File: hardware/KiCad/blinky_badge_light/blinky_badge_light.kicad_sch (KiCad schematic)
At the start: 12 parts, among them U1 ESP32-S3-WROOM-1

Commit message: updated schematic to use 'basic' parts from jlcpcb where I could
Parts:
- C39: JLCPCB Part # C2762594 -> C59461
- C40: JLCPCB Part # C1848 -> C15849
- R1: JLCPCB Part # C105882 -> C22775
- R11, R12: JLCPCB Part # C98220 -> C25804
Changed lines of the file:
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@@
 			)
 		)
-		(property "Datasheet" "https://www.lcsc.com/datasheet/lcsc_datasheet_2304140030_Samsung-Electro-Mechanics-CL31B105KBHNNNE_C1848.pdf"
+		(property "Datasheet" "https://jlcpcb.com/api/file/downloadByFileSystemAccessId/8556213788459761664"
 			(at 88.9 48.26 0)
 			(effects
@@
 			)
 		)
-		(property "JLCPCB Part #" "C1848"
+		(property "JLCPCB Part #" "C15849"
 			(at 88.9 48.26 0)
 			(effects
@@
 			)
 		)
-		(property "Datasheet" "https://www.lcsc.com/datasheet/lcsc_datasheet_2304140030_YAGEO-RC0603FR-0710KL_C98220.pdf"
+		(property "Datasheet" "https://jlcpcb.com/api/file/downloadByFileSystemAccessId/8579706381320323072"
 			(at 224.79 63.5 0)
 			(effects
@@
 			)
 		)
-		(property "JLCPCB Part #" "C98220"
+		(property "JLCPCB Part #" "C25804"
 			(at 224.79 63.5 0)
 			(effects
@@
 			)
 		)
-		(property "Datasheet" "https://www.lcsc.com/datasheet/lcsc_datasheet_2304140030_YAGEO-RC0603FR-0710KL_C98220.pdf"
+		(property "Datasheet" "https://jlcpcb.com/api/file/downloadByFileSystemAccessId/8579706381320323072"
 			(at 105.41 45.72 0)
 			(effects
@@
 			)
 		)
-		(property "JLCPCB Part #" "C98220"
+		(property "JLCPCB Part #" "C25804"
 			(at 105.41 45.72 0)
 			(effects
@@
 			)
 		)
-		(property "Datasheet" "https://www.lcsc.com/datasheet/lcsc_datasheet_2208111030_Samsung-Electro-Mechanics-CL10A226MO7JZNC_C2762594.pdf"
+		(property "Datasheet" "https://jlcpcb.com/api/file/downloadByFileSystemAccessId/8555544417670705152"
 			(at 128.27 30.48 0)
 			(effects
@@
 			)
 		)
-		(property "JLCPCB Part #" "C2762594"
+		(property "JLCPCB Part #" "C59461"
 			(at 128.27 30.48 0)
 			(effects
@@
 			)
 		)
-		(property "Datasheet" "https://www.lcsc.com/datasheet/lcsc_datasheet_2407081117_YAGEO-CC0402KRX5R9BB104_C105882.pdf"
+		(property "Datasheet" "https://jlcpcb.com/api/file/downloadByFileSystemAccessId/8579706114222985216"
 			(at 218.44 76.2 0)
 			(effects
@@
 			)
 		)
-		(property "JLCPCB Part #" "C105882"
+		(property "JLCPCB Part #" "C22775"
 			(at 218.44 76.2 0)
 			(effects

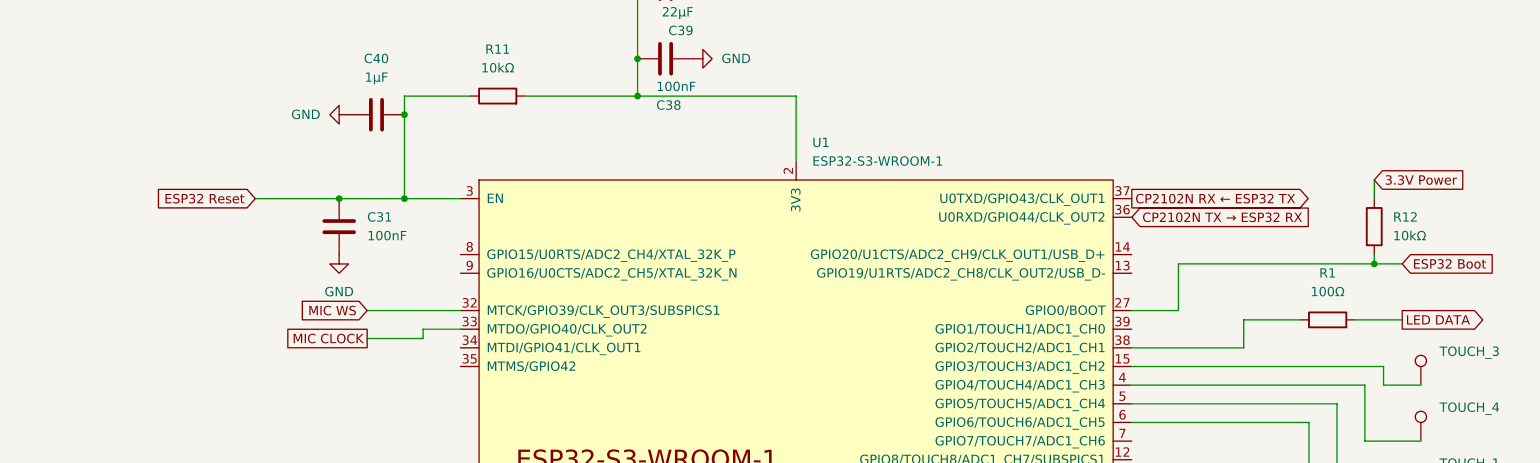
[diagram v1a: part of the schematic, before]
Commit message: swap esp32 boot and reset's connections to CP2102
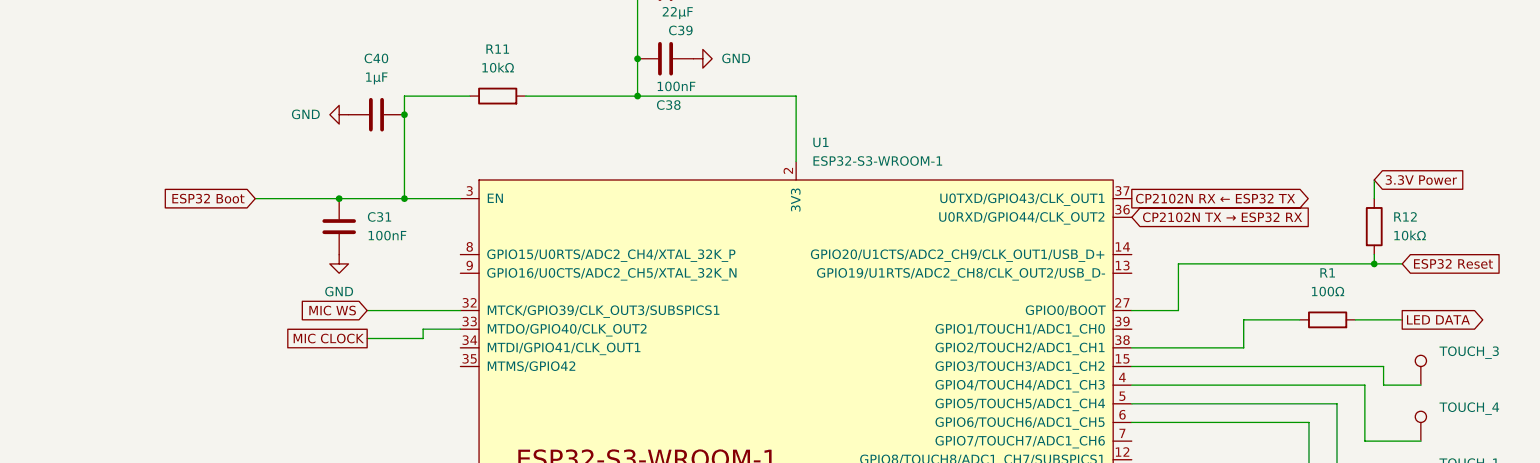
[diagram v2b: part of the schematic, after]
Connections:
- net ESP32 Boot: now also C31.2, C40.2, R11.1, U1.3 (EN); no longer R12.2, U1.27 (GPIO0/BOOT)
- net ESP32 Reset: now also R12.2, U1.27 (GPIO0/BOOT); no longer C31.2, C40.2, R11.1, U1.3 (EN)
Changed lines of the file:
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@@
 		)
 	)
-	(global_label "ESP32 Boot"
+	(global_label "ESP32 Reset"
 		(shape input)
 		(at 228.6 68.58 0)
@@
 		)
 		(property "Intersheetrefs" "${INTERSHEET_REFS}"
-			(at 242.894 68.58 0)
+			(at 243.8013 68.58 0)
 			(effects
 				(font
@@
 		)
 	)
-	(global_label "ESP32 Reset"
+	(global_label "ESP32 Boot"
 		(shape input)
 		(at 72.39 59.69 180)
@@
 		)
 		(property "Intersheetrefs" "${INTERSHEET_REFS}"
-			(at 57.1887 59.69 0)
+			(at 58.096 59.69 0)
 			(effects
 				(font

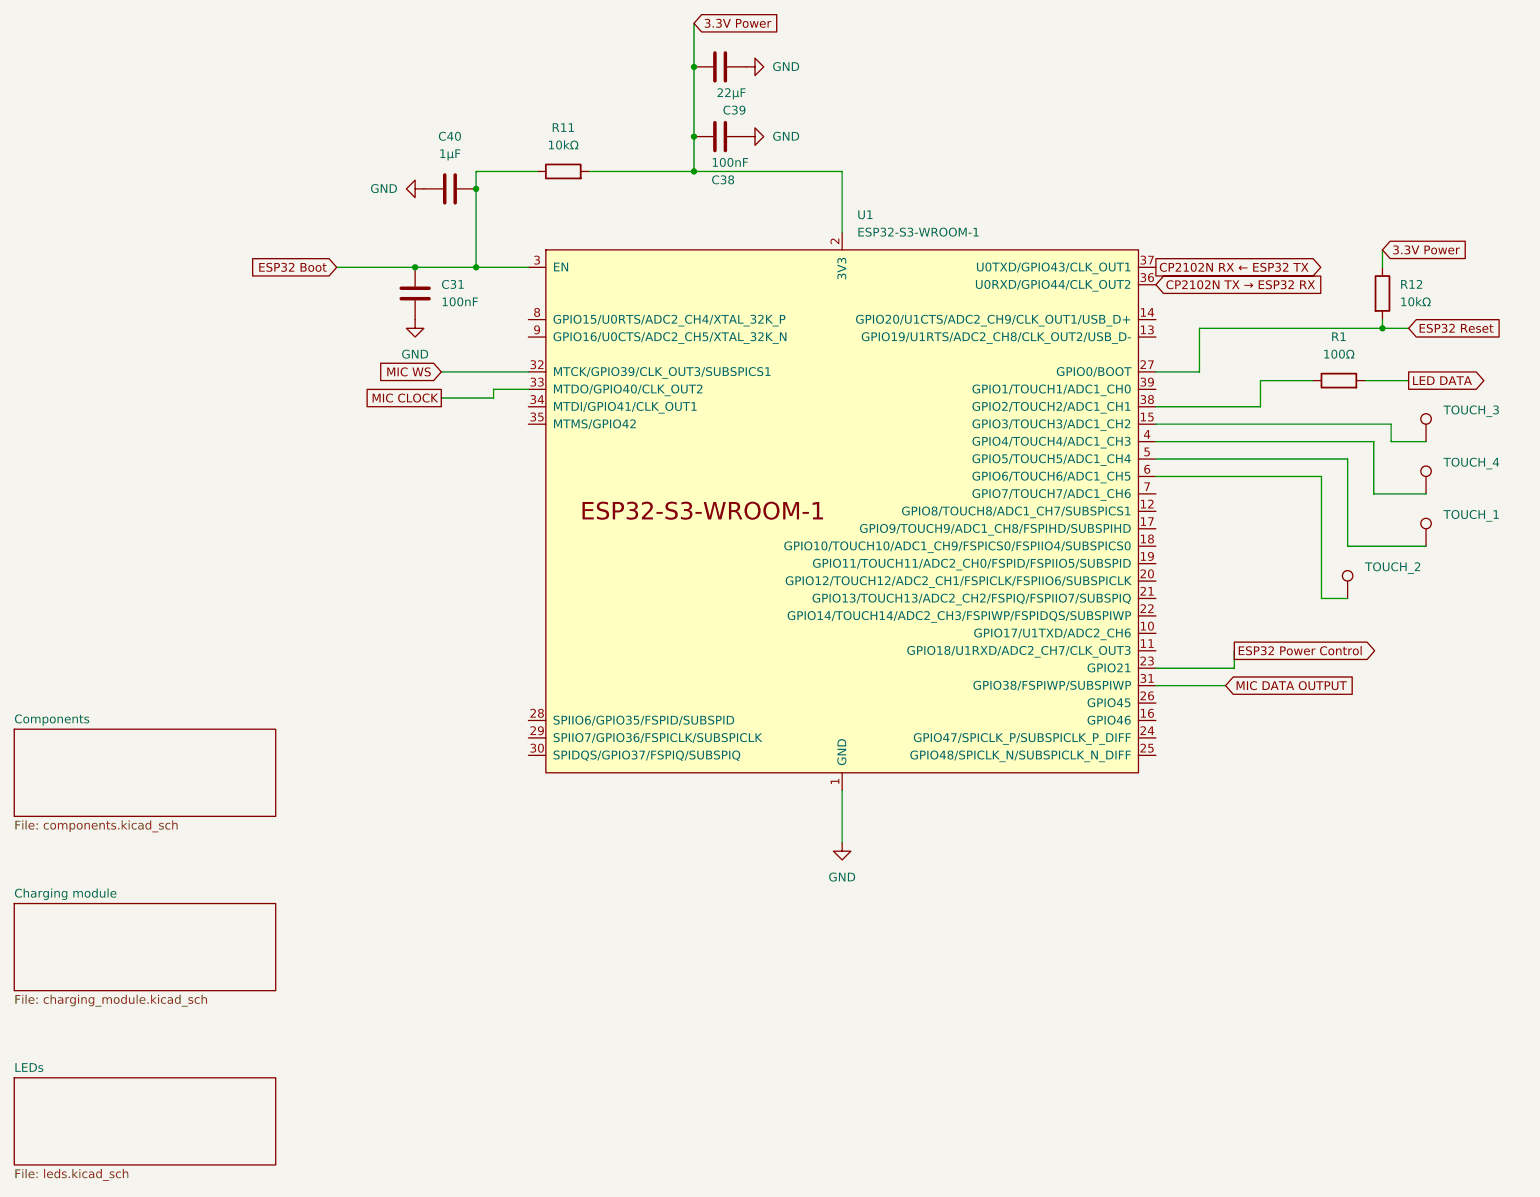
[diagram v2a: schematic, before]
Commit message: added battery polarity protection and charging monitoring circuit
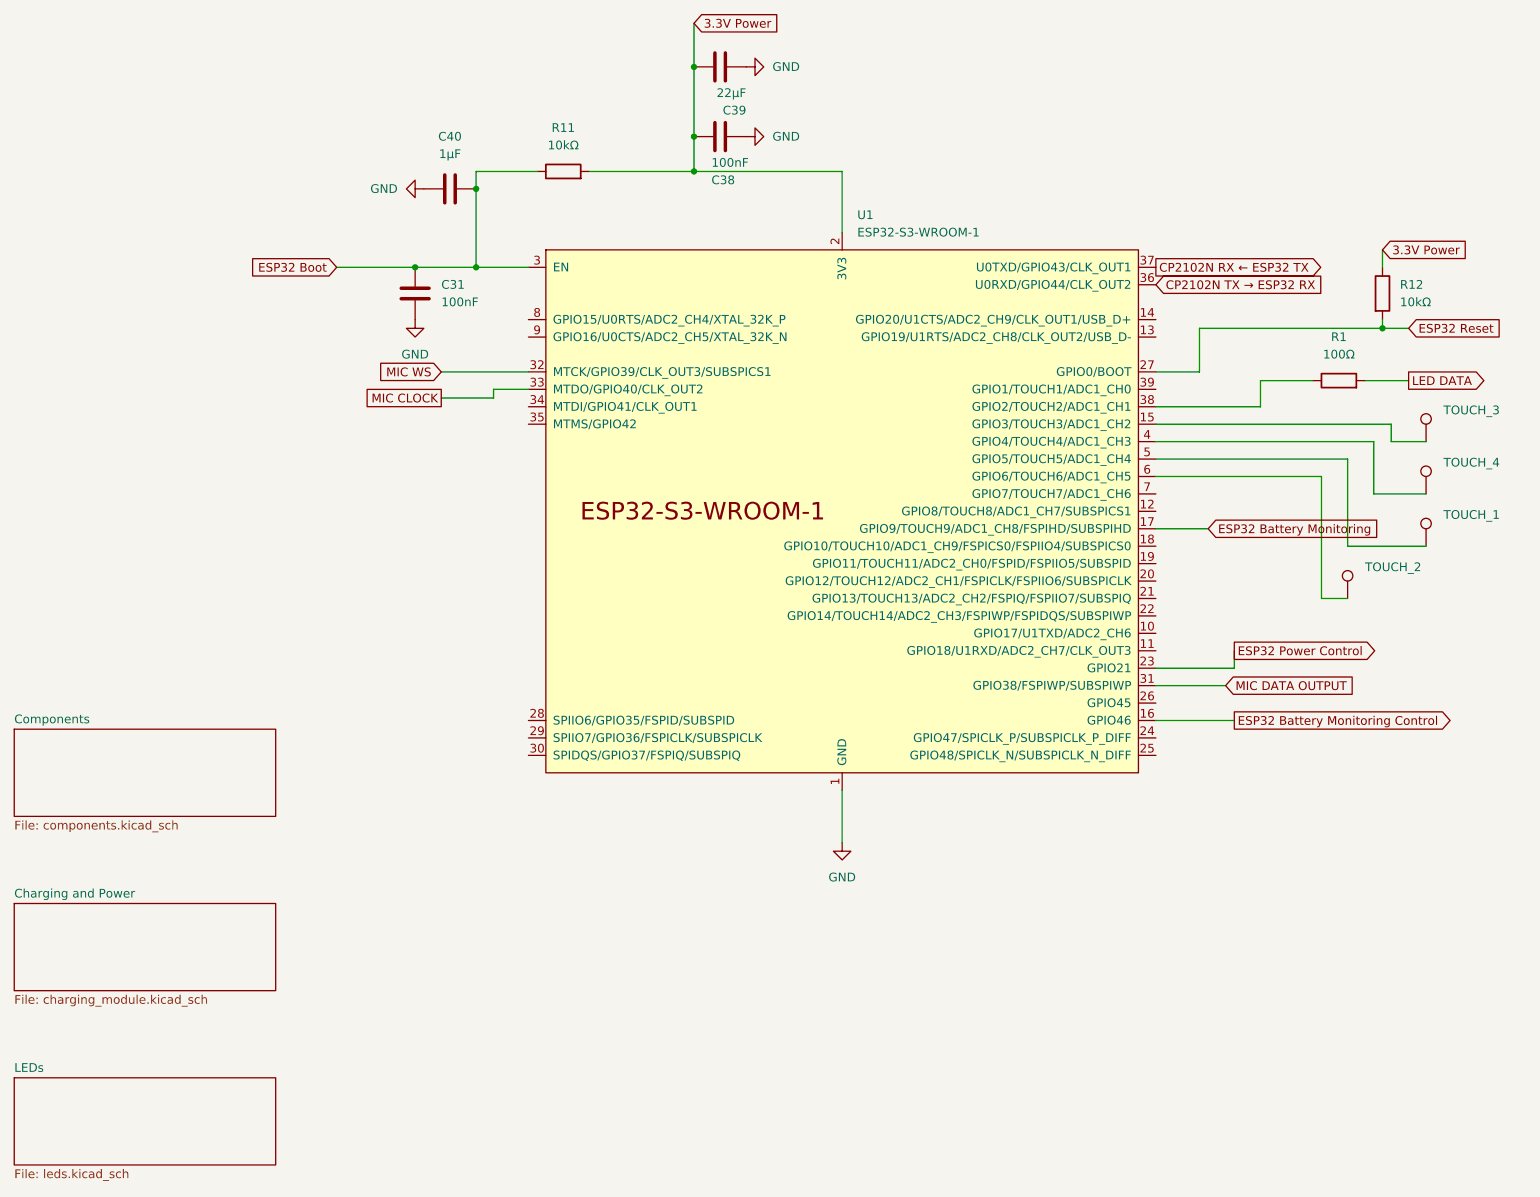
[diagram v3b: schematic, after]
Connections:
- net ESP32 Battery Monitoring Control: now reaches U1.16 (GPIO46)
- net ESP32 Battery Monitoring: now reaches U1.17 (GPIO9/TOUCH9/ADC1_CH8/FSPIHD/SUBSPIHD)
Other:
- sheet Charging module renamed Charging and Power
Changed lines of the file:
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@@
+	(wire
+		(pts
+			(xy 191.77 125.73) (xy 203.2 125.73)
+		)
+		(stroke
+			(width 0)
+			(type default)
+		)
+	)
 	(wire
 		(pts
@@
 		(pts
 			(xy 207.01 80.01) (xy 191.77 80.01)
+		)
+		(stroke
+			(width 0)
+			(type default)
+		)
+	)
+	(wire
+		(pts
+			(xy 191.77 97.79) (xy 199.39 97.79)
 		)
 		(stroke
@@
 		)
 	)
+	(global_label "ESP32 Battery Monitoring Control"
+		(shape output)
+		(at 203.2 125.73 0)
+		(fields_autoplaced yes)
+		(effects
+			(font
+				(size 1.27 1.27)
+			)
+			(justify left)
+		)
+		(property "Intersheetrefs" "${INTERSHEET_REFS}"
+			(at 238.6603 125.73 0)
+			(effects
+				(font
+					(size 1.27 1.27)
+				)
+				(justify left)
+				(hide yes)
+			)
+		)
+	)
 	(global_label "LED DATA"
 		(shape output)
@@
 		(property "Intersheetrefs" "${INTERSHEET_REFS}"
 			(at 221.7881 120.65 0)
+			(effects
+				(font
+					(size 1.27 1.27)
+				)
+				(justify left)
+				(hide yes)
+			)
+		)
+	)
+	(global_label "ESP32 Battery Monitoring"
+		(shape input)
+		(at 199.39 97.79 0)
+		(fields_autoplaced yes)
+		(effects
+			(font
+				(size 1.27 1.27)
+			)
+			(justify left)
+		)
+		(property "Intersheetrefs" "${INTERSHEET_REFS}"
+			(at 226.9886 97.79 0)
 			(effects
 				(font
@@
 			(color 0 0 0 0.0000)
 		)
-		(property "Sheetname" "Charging module"
+		(property "Sheetname" "Charging and Power"
 			(at 25.4 151.6884 0)
 			(effects

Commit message: moving some stuff around
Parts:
- added TOUCH_5: TestPoint, TestPoint:TestPoint_Pad_D4.0mm, symbol Connector:TestPoint
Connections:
- net at U1.7 (GPIO7/TOUCH7/ADC1_CH6): now also TOUCH_5.1
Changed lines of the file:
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@@
+	(wire
+		(pts
+			(xy 191.77 92.71) (xy 196.85 92.71)
+		)
+		(stroke
+			(width 0)
+			(type default)
+		)
+	)
 	(wire
 		(pts
@@
 					(unit 1)
 				)
+			)
+		)
+	)
+	(symbol
+		(lib_id "Connector:TestPoint")
+		(at 196.85 92.71 270)
+		(unit 1)
+		(exclude_from_sim no)
+		(in_bom yes)
+		(on_board yes)
+		(dnp no)
+		(property "Reference" "TOUCH_5"
+			(at 201.93 92.71 90)
+			(effects
+				(font
+					(size 1.27 1.27)
+				)
+				(justify left)
+			)
+		)
+		(property "Value" "TestPoint"
+			(at 201.93 93.9799 90)
+			(effects
+				(font
+					(size 1.27 1.27)
+				)
+				(justify left)
+				(hide yes)
+			)
+		)
+		(property "Footprint" "TestPoint:TestPoint_Pad_D4.0mm"
+			(at 196.85 97.79 0)
+			(effects
+				(font
+					(size 1.27 1.27)
+				)
+				(hide yes)
+			)
+		)
+		(property "Datasheet" "~"
+			(at 196.85 97.79 0)
+			(effects
+				(font
+					(size 1.27 1.27)
+				)
+				(hide yes)
+			)
+		)
+		(property "Description" "test point"
+			(at 196.85 92.71 0)
+			(effects
+				(font
+					(size 1.27 1.27)
+				)
+				(hide yes)
+			)
+		)
+		(pin "1"
+		)
+		(instances
+			(project ""
+				(path "/f33039b1-b38b-4cb6-baf0-07a137773378"
+					(reference "TOUCH_5")
+					(unit 1)
+				)

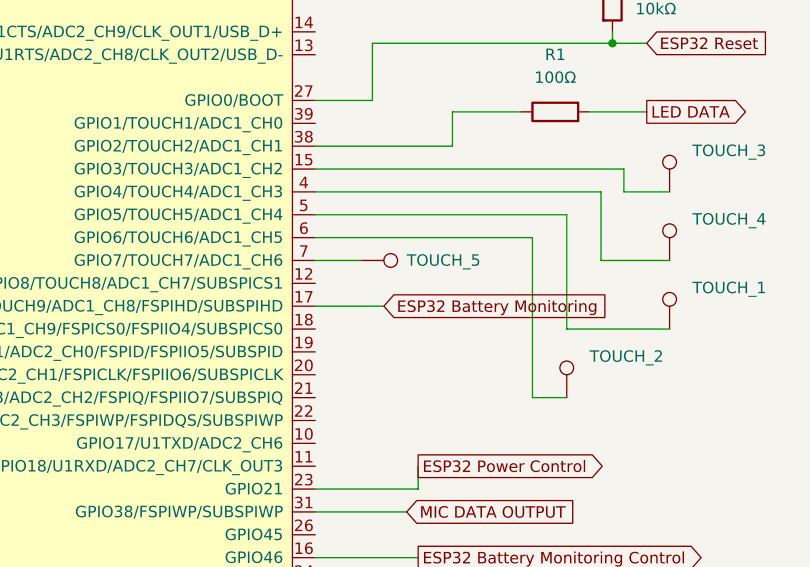
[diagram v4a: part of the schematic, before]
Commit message: adding two new touch pads
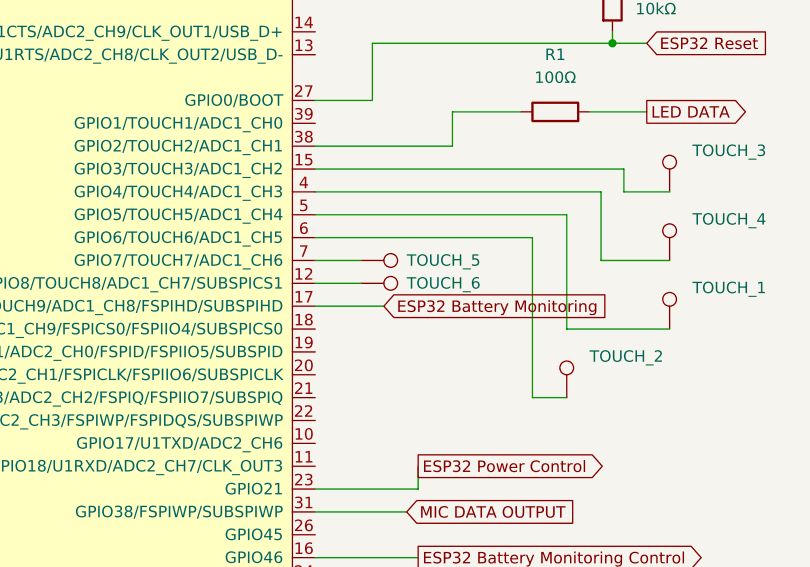
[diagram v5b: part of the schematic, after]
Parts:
- added TOUCH_6: TestPoint, footprints:TestPoint_Pad_D7.0mm, symbol Connector:TestPoint
- TOUCH_5: footprint TestPoint:TestPoint_Pad_D4.0mm -> footprints:TestPoint_Pad_D7.0mm
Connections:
- net at U1.12 (GPIO8/TOUCH8/ADC1_CH7/SUBSPICS1): now also TOUCH_6.1
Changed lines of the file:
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@@
+	(wire
+		(pts
+			(xy 191.77 95.25) (xy 196.85 95.25)
+		)
+		(stroke
+			(width 0)
+			(type default)
+		)
+	)
 	(wire
 		(pts
@@
 			)
 		)
-		(property "Footprint" "TestPoint:TestPoint_Pad_D4.0mm"
+		(property "Footprint" "footprints:TestPoint_Pad_D7.0mm"
 			(at 196.85 97.79 0)
 			(effects
@@
 					(unit 1)
 				)
+			)
+		)
+	)
+	(symbol
+		(lib_id "Connector:TestPoint")
+		(at 196.85 95.25 270)
+		(unit 1)
+		(exclude_from_sim no)
+		(in_bom yes)
+		(on_board yes)
+		(dnp no)
+		(fields_autoplaced yes)
+		(property "Reference" "TOUCH_6"
+			(at 201.93 95.2499 90)
+			(effects
+				(font
+					(size 1.27 1.27)
+				)
+				(justify left)
+			)
+		)
+		(property "Value" "TestPoint"
+			(at 201.93 96.5199 90)
+			(effects
+				(font
+					(size 1.27 1.27)
+				)
+				(justify left)
+				(hide yes)
+			)
+		)
+		(property "Footprint" "footprints:TestPoint_Pad_D7.0mm"
+			(at 196.85 100.33 0)
+			(effects
+				(font
+					(size 1.27 1.27)
+				)
+				(hide yes)
+			)
+		)
+		(property "Datasheet" "~"
+			(at 196.85 100.33 0)
+			(effects
+				(font
+					(size 1.27 1.27)
+				)
+				(hide yes)
+			)
+		)
+		(property "Description" "test point"
+			(at 196.85 95.25 0)
+			(effects
+				(font
+					(size 1.27 1.27)
+				)
+				(hide yes)
+			)
+		)
+		(pin "1"
+		)
+		(instances
+			(project ""
+				(path "/f33039b1-b38b-4cb6-baf0-07a137773378"
+					(reference "TOUCH_6")
+					(unit 1)
+				)

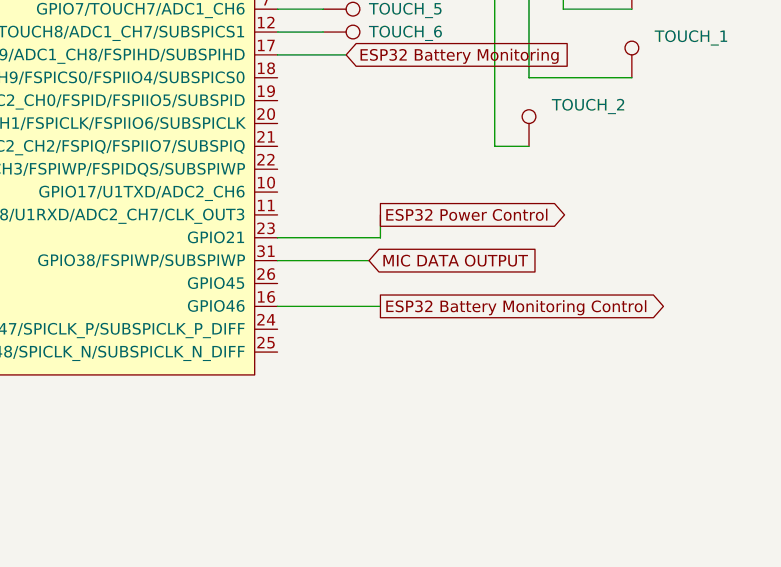
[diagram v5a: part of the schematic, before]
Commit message: here's an idea.. use schottkey diode so we can detect presses after it's turned on?
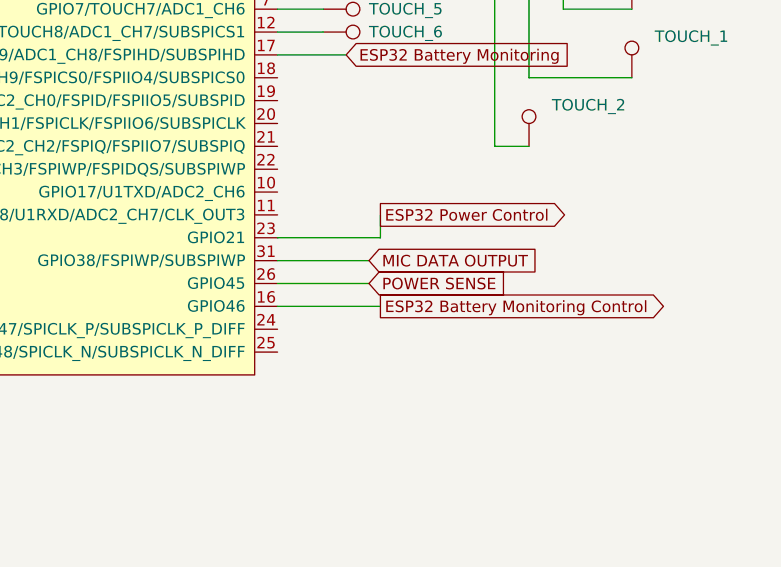
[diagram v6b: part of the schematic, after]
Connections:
- net POWER SENSE: now reaches U1.26 (GPIO45)
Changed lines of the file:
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@@
+	(wire
+		(pts
+			(xy 191.77 123.19) (xy 201.93 123.19)
+		)
+		(stroke
+			(width 0)
+			(type default)
+		)
+	)
 	(wire
 		(pts
@@
 			(effects
 				(font
+					(size 1.27 1.27)
+				)
+				(justify left)
+				(hide yes)
+			)
+		)
+	)
+	(global_label "POWER SENSE"
+		(shape input)
+		(at 201.93 123.19 0)
+		(fields_autoplaced yes)
+		(effects
+			(font
+				(size 1.27 1.27)
+			)
+			(justify left)
+		)
+		(property "Intersheetrefs" "${INTERSHEET_REFS}"
+			(at 218.4012 123.19 0)
+			(effects
+				(font
